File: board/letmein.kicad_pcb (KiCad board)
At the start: 2 copper layers, 61 x 43.2 mm, 26 parts

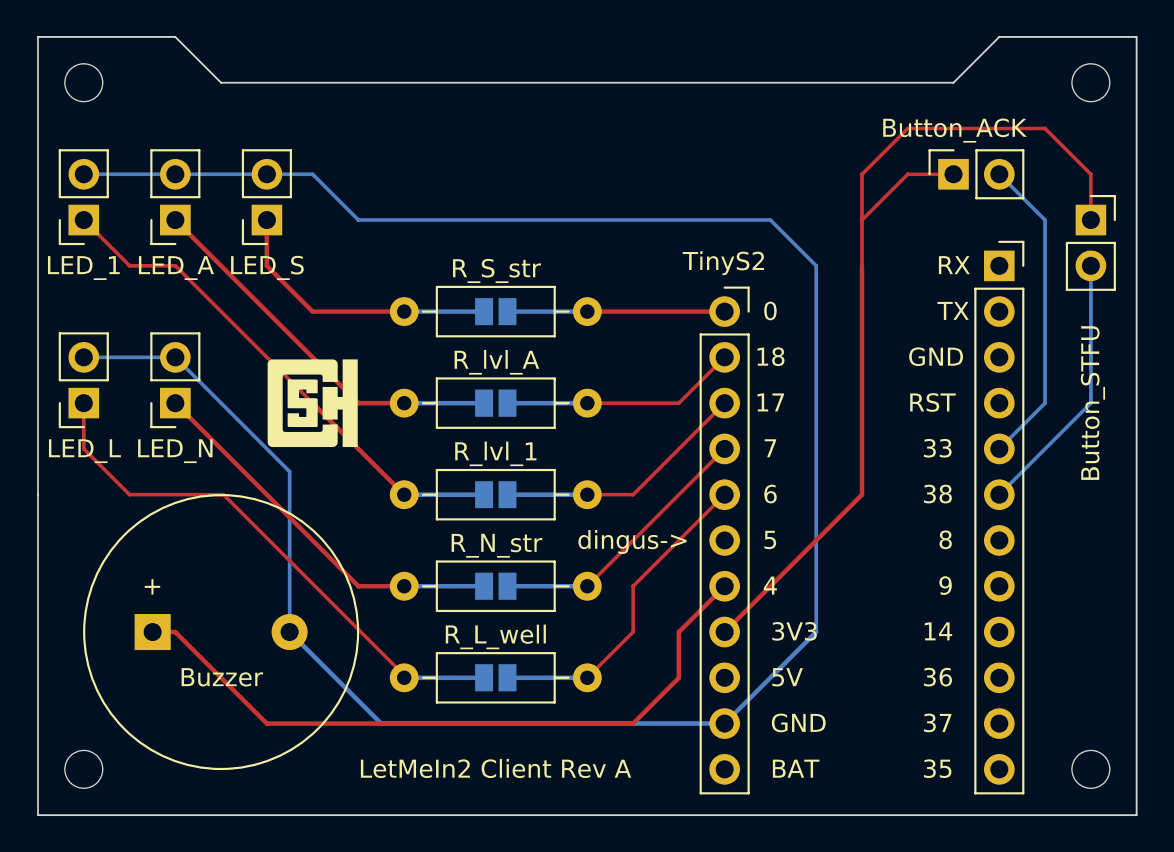
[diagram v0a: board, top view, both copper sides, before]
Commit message: Shrink board, move headers
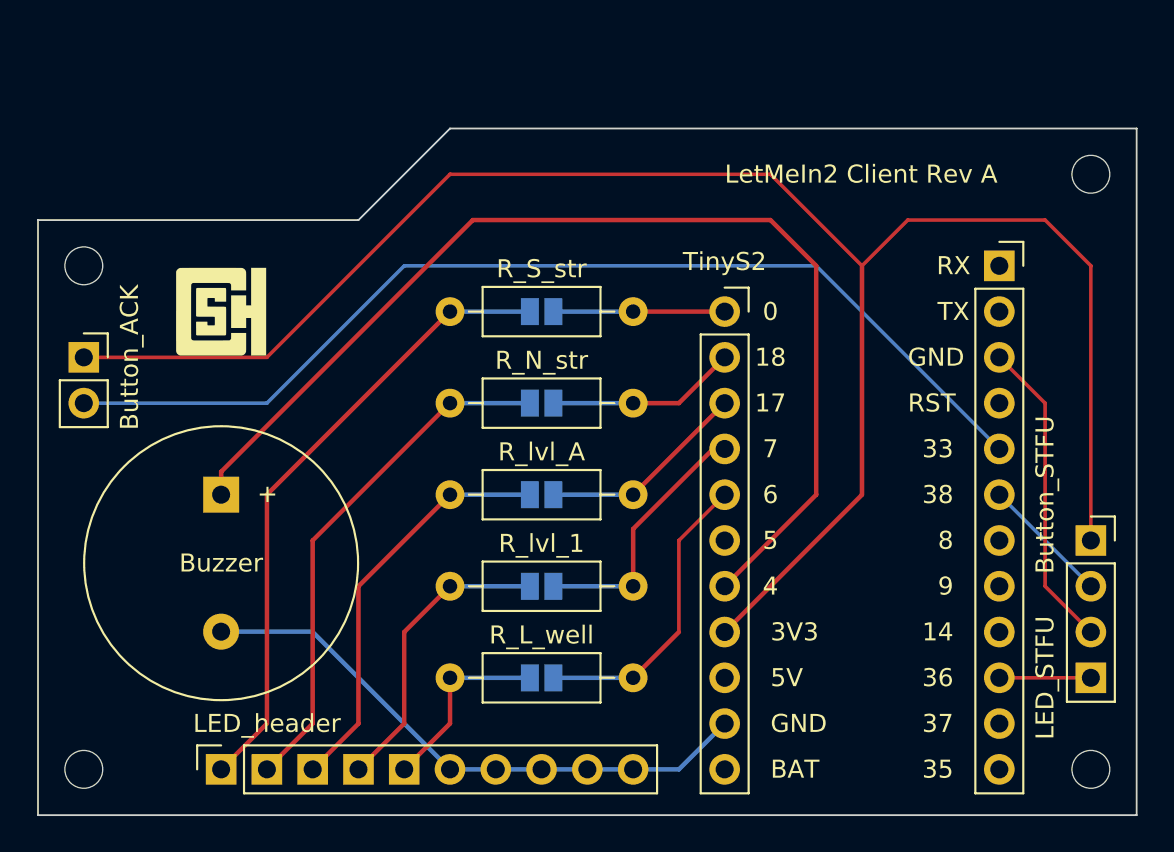
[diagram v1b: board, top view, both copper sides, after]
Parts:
- removed Button_STFU, LED_1, LED_A, LED_L, LED_N, LED_S: PinSocket_1x02_P2.54mm_Vertical, Connector_PinSocket_2.54mm:PinSocket_1x02_P2.54mm_Vertical
- added LED_STFU: PinSocket_1x04_P2.54mm_Vertical, Connector_PinSocket_2.54mm:PinSocket_1x04_P2.54mm_Vertical, F.Cu at (165.1, 91.4)
- added LED_header: PinSocket_1x10_P2.54mm_Vertical, Connector_PinSocket_2.54mm:PinSocket_1x10_P2.54mm_Vertical, F.Cu at (116.8, 104.1)
- moved Button_ACK 49.3 mm to (109.2, 81.3), turned to 0 degrees
- moved REF** 10.2 mm to (109.2, 76.2)
- moved Buzzer 8.51 mm to (116.8, 88.9), turned to -90 degrees
- moved G*** 7.18 mm to (116.8, 78.7)
- moved REF** 5.08 mm to (165.1, 71.1)
- moved G*** 2.54 mm to (116.8, 94.0)
- moved REF** 2.54 mm to (134.6, 78.7)
- moved REF** 2.54 mm to (134.6, 83.8)
- moved REF** 2.54 mm to (134.6, 99.1)
- moved REF** 2.54 mm to (134.6, 94.0)
- moved REF** 2.54 mm to (134.6, 88.9)
- moved R_L_well 2.54 mm to (129.5, 99.1)
- moved R_N_str 2.54 mm to (129.5, 83.8)
- moved R_S_str 2.54 mm to (129.5, 78.7)
- moved R_lvl_1 2.54 mm to (129.5, 94.0)
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- renumbered R_lvl_A to R_N_str, R_N_str to R_lvl_1, R_lvl_1 to R_lvl_A
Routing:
- net (no net): track 431.4 -> 461.0 mm
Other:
- board size 61 x 43.2 mm -> 61 x 38.1 mm
- board text added: "<-Fuck you Noah :)"
- board text added: "<-dingus"
- board text added: "Button_STFU"
- board text removed: "Fuck you Noah :) ->"
- board text removed: "dingus->"

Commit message: Change LED connector style. WIP.
I guess this is the start of Rev B. I realized that I could
probably standardize the ribbon cable. In theory, I could also create a
PCB for the front panel LEDs, then use a standard 2x5-pin ribbon cable
to connect the two boards.

Damn, that'd be a great idea.
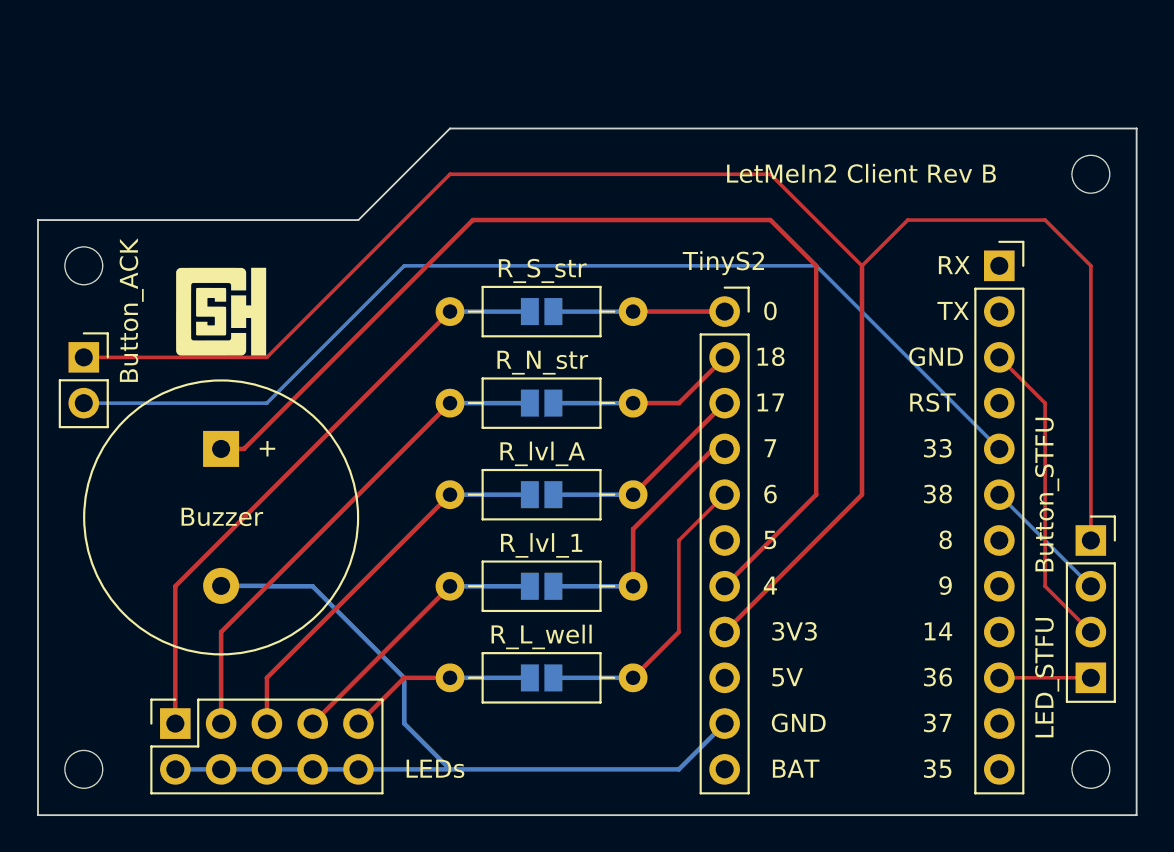
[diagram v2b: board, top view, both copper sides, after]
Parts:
- removed LED_header: PinSocket_1x10_P2.54mm_Vertical, Connector_PinSocket_2.54mm:PinSocket_1x10_P2.54mm_Vertical
- added LEDs: PinSocket_2x05_P2.54mm_Vertical, Connector_PinSocket_2.54mm:PinSocket_2x05_P2.54mm_Vertical, F.Cu at (114.3, 101.6)
- moved Buzzer 2.54 mm to (116.8, 86.4)
- turned REF** to 90 degrees
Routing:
- net (no net): track 461.0 -> 471.0 mm
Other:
- board text added: "LetMeIn2 Client Rev B"
- board text removed: "LetMeIn2 Client Rev A"
